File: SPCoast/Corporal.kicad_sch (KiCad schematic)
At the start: 36 parts, among them SW11829 829, SW11831 831, SW11900 829D, SW11901 1

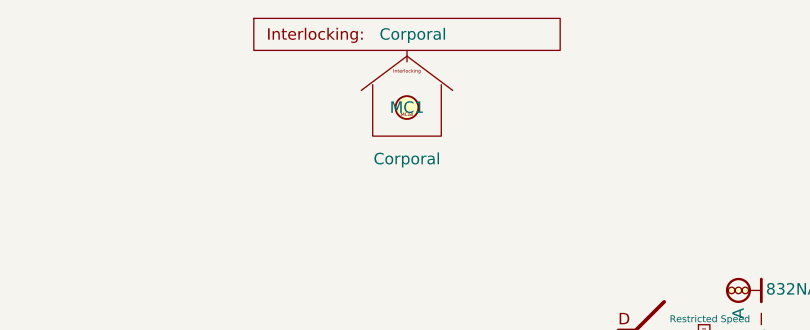
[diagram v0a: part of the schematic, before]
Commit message: chore(kicad): owner mockup: explicit seam wiring on Luchessa and South-cTc, host and bus pins
Owner's edits, committed as they stand (2026-10-21), before scripted edits build on them.

- Interlocking gains Codeline and Host pins; MAIN HOUSE's Interlocking pin is Codeline.
- OfficeUnit gains Host and Codeline pins; JohnCTC desk processor drawn on South-cTc.
- Processor gains Transport and IO pins; MAX7313 and MCP23017 gain an I2C bus pin.
- Transports: Codeline pin renamed Host; JMRI_MQTT instance added; Loconet removed.
- Encodings' pin renamed Transport; Luchessa's 506 and Bit Packing instances removed.
- SPCoastApp virtual host (FieldUnit_Virtual) hosts CMRInet and JMRI_MQTT.
- Luchessa: unit, houses and Time Coded on one net; Host to its own processor;
  panel MAX7313s on the desk bus (OfficeBus).
- Watsonville, Caltrain, Interchange: first-pass Processor placeholders, to be redrawn.

Verified: netlist and ERC exported from the saved project; field diff against the
committed netlist shows no per-instance field lost.
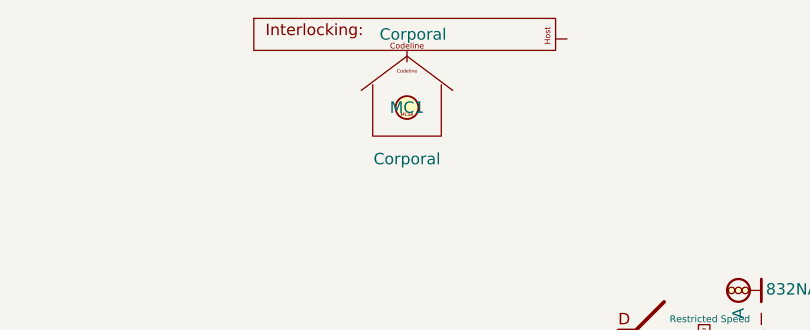
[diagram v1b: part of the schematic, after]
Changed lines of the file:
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@@
 		(pin "1"
+		)
+		(pin "2"
 		)
 		(instances
